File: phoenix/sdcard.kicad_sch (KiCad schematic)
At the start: 4 parts, among them U5 XTSD04G

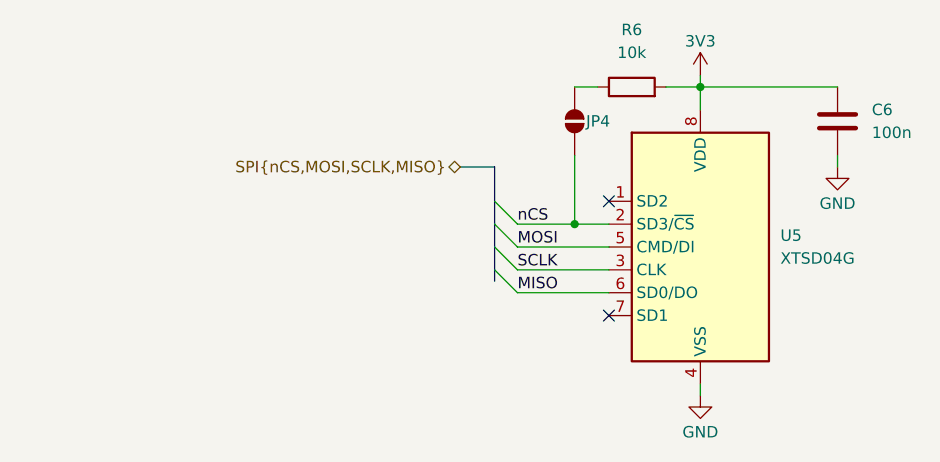
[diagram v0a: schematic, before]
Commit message: Finished schematics and almost done layouts of LC26 PCBs
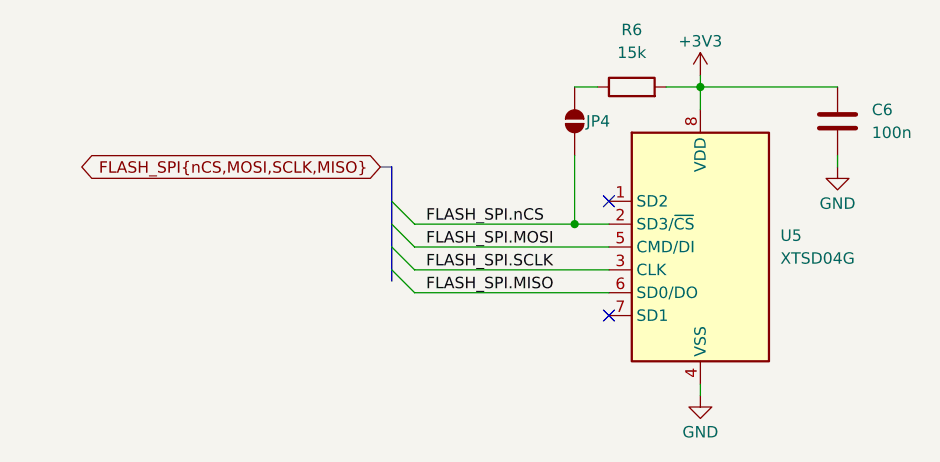
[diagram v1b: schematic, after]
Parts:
- C6: footprint (none) -> Capacitor_SMD:C_0603_1608Metric_Pad1.08x0.95mm_HandSolder
- JP4: footprint (none) -> Jumper:SolderJumper-2_P1.3mm_Open_Pad1.0x1.5mm
- R6: value 10k -> 15k; footprint (none) -> Resistor_SMD:R_0603_1608Metric_Pad0.98x0.95mm_HandSolder
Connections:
- net 3V3 renamed +3V3
- net MISO renamed FLASH_SPI.MISO
- net MOSI renamed FLASH_SPI.MOSI
- net SCLK renamed FLASH_SPI.SCLK
- net nCS renamed FLASH_SPI.nCS
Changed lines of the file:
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@@
 	)
 	(bus_entry
-		(at 82.55 71.12)
+		(at 71.12 78.74)
 		(size 2.54 2.54)
 		(stroke
@@
 	)
 	(bus_entry
-		(at 82.55 73.66)
+		(at 71.12 73.66)
 		(size 2.54 2.54)
 		(stroke
@@
 	)
 	(bus_entry
-		(at 82.55 76.2)
+		(at 71.12 76.2)
 		(size 2.54 2.54)
 		(stroke
@@
 	)
 	(bus_entry
-		(at 82.55 78.74)
+		(at 71.12 71.12)
 		(size 2.54 2.54)
 		(stroke
@@
 		)
 	)
+	(wire
+		(pts
+			(xy 73.66 81.28) (xy 95.25 81.28)
+		)
+		(stroke
+			(width 0)
+			(type default)
+		)
+	)
 	(bus
 		(pts
-			(xy 78.74 67.31) (xy 82.55 67.31)
+			(xy 69.85 67.31) (xy 71.12 67.31)
+		)
+		(stroke
+			(width 0)
+			(type default)
+		)
+	)
+	(wire
+		(pts
+			(xy 73.66 78.74) (xy 95.25 78.74)
 		)
 		(stroke
@@
 	(bus
 		(pts
-			(xy 82.55 78.74) (xy 82.55 80.01)
+			(xy 71.12 73.66) (xy 71.12 76.2)
+		)
+		(stroke
+			(width 0)
+			(type default)
+		)
+	)
+	(wire
+		(pts
+			(xy 73.66 73.66) (xy 91.44 73.66)
+		)
+		(stroke
+			(width 0)
+			(type default)
+		)
+	)
+	(wire
+		(pts
+			(xy 101.6 58.42) (xy 105.41 58.42)
 		)
 		(stroke
@@
 	(bus
 		(pts
-			(xy 82.55 76.2) (xy 82.55 78.74)
-		)
-		(stroke
-			(width 0)
-			(type default)
-		)
-	)
-	(wire
-		(pts
-			(xy 101.6 58.42) (xy 105.41 58.42)
+			(xy 71.12 67.31) (xy 71.12 71.12)
+		)
+		(stroke
+			(width 0)
+			(type default)
+		)
+	)
+	(wire
+		(pts
+			(xy 105.41 92.71) (xy 105.41 91.44)
+		)
+		(stroke
+			(width 0)
+			(type default)
+		)
+	)
+	(wire
+		(pts
+			(xy 120.65 67.31) (xy 120.65 66.04)
+		)
+		(stroke
+			(width 0)
+			(type default)
+		)
+	)
+	(wire
+		(pts
+			(xy 91.44 73.66) (xy 95.25 73.66)
 		)
 		(stroke
@@
 	(bus
 		(pts
-			(xy 82.55 67.31) (xy 82.55 71.12)
-		)
-		(stroke
-			(width 0)
-			(type default)
-		)
-	)
-	(wire
-		(pts
-			(xy 105.41 92.71) (xy 105.41 91.44)
-		)
-		(stroke
-			(width 0)
-			(type default)
-		)
-	)
-	(wire
-		(pts
-			(xy 120.65 67.31) (xy 120.65 66.04)
-		)
-		(stroke
-			(width 0)
-			(type default)
-		)
-	)
-	(wire
-		(pts
-			(xy 91.44 73.66) (xy 95.25 73.66)
+			(xy 71.12 76.2) (xy 71.12 78.74)
 		)
 		(stroke
@@
 	(wire
 		(pts
-			(xy 85.09 76.2) (xy 95.25 76.2)
-		)
-		(stroke
-			(width 0)
-			(type default)
-		)
-	)
-	(wire
-		(pts
 			(xy 105.41 58.42) (xy 105.41 60.96)
 		)
@@
 	(wire
 		(pts
-			(xy 85.09 78.74) (xy 95.25 78.74)
-		)
-		(stroke
-			(width 0)
-			(type default)
-		)
-	)
-	(wire
-		(pts
-			(xy 85.09 81.28) (xy 95.25 81.28)
-		)
-		(stroke
-			(width 0)
-			(type default)
-		)
-	)
-	(wire
-		(pts
-			(xy 85.09 73.66) (xy 91.44 73.66)
-		)
-		(stroke
-			(width 0)
-			(type default)
-		)
-	)
-	(wire
-		(pts
 			(xy 105.41 57.15) (xy 105.41 58.42)
 		)
@@
 	(bus
 		(pts
-			(xy 82.55 73.66) (xy 82.55 76.2)
+			(xy 71.12 78.74) (xy 71.12 80.01)
+		)
+		(stroke
+			(width 0)
+			(type default)
+		)
+	)
+	(wire
+		(pts
+			(xy 73.66 76.2) (xy 95.25 76.2)
 		)
 		(stroke
@@
 	(bus
 		(pts
-			(xy 82.55 71.12) (xy 82.55 73.66)
-		)
-		(stroke
-			(width 0)
-			(type default)
-		)
-	)
-	(label "nCS"
-		(at 85.09 73.66 0)
+			(xy 71.12 71.12) (xy 71.12 73.66)
+		)
+		(stroke
+			(width 0)
+			(type default)
+		)
+	)
+	(label "FLASH_SPI.SCLK"
+		(at 74.93 78.74 0)
 		(effects
 			(font
@@
 		)
 	)
-	(label "SCLK"
-		(at 85.09 78.74 0)
+	(label "FLASH_SPI.MISO"
+		(at 74.93 81.28 0)
 		(effects
 			(font
@@
 		)
 	)
-	(label "MISO"
-		(at 85.09 81.28 0)
+	(label "FLASH_SPI.MOSI"
+		(at 74.93 76.2 0)
 		(effects
 			(font
@@
 		)
 	)
-	(label "MOSI"
-		(at 85.09 76.2 0)
+	(label "FLASH_SPI.nCS"
+		(at 74.93 73.66 0)
 		(effects
 			(font
@@
 		)
 	)
-	(hierarchical_label "SPI{nCS,MOSI,SCLK,MISO}"
+	(global_label "FLASH_SPI{nCS,MOSI,SCLK,MISO}"
 		(shape bidirectional)
-		(at 78.74 67.31 180)
+		(at 69.85 67.31 180)
+		(fields_autoplaced yes)
 		(effects
 			(font
@@
 			)
 			(justify right)
+		)
+		(property "Intersheetrefs" "${INTERSHEET_REFS}"
+			(at 34.85 67.31 0)
+			(effects
+				(font
+					(size 1.27 1.27)
+				)
+				(justify right)
+				(hide yes)
+			)
 		)
 	)
@@
 			)
 		)
-		(property "Footprint" ""
+		(property "Footprint" "Jumper:SolderJumper-2_P1.3mm_Open_Pad1.0x1.5mm"
 			(at 91.44 62.23 0)
 			(effects
@@
 			)
 		)
-		(property "Value" "10k"
+		(property "Value" "15k"
 			(at 97.79 54.61 90)
 			(effects
@@
 			)
 		)
-		(property "Footprint" ""
+		(property "Footprint" "Resistor_SMD:R_0603_1608Metric_Pad0.98x0.95mm_HandSolder"
 			(at 97.79 60.198 90)
 			(effects
@@
 			)
 		)
-		(property "Footprint" ""
+		(property "Footprint" "Capacitor_SMD:C_0603_1608Metric_Pad1.08x0.95mm_HandSolder"
 			(at 121.6152 66.04 0)
 			(effects
@@
 			)
 		)
-		(property "Value" "3V3"
+		(property "Value" "+3V3"
 			(at 105.41 53.34 0)
 			(effects
